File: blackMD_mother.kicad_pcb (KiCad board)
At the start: 2 copper layers, 99.1 x 99.1 mm, 19 parts

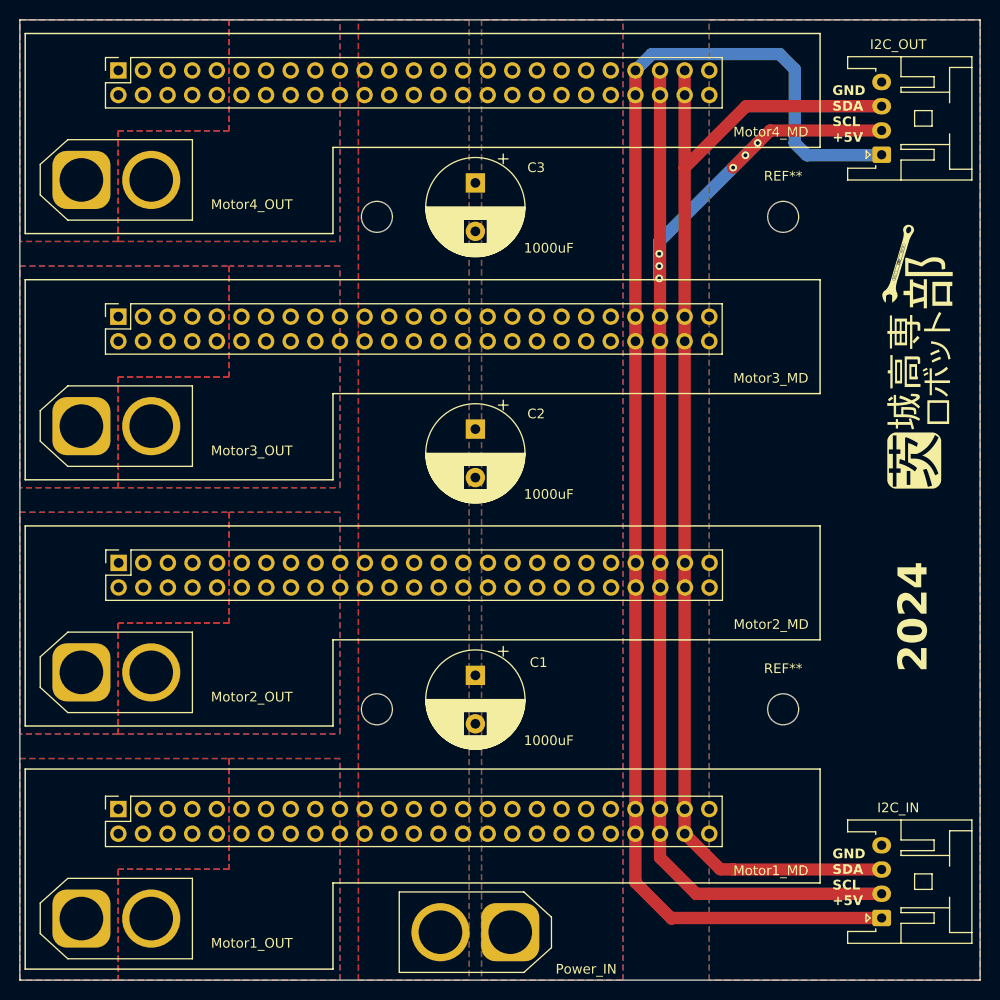
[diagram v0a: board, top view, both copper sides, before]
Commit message: change: fillet corners
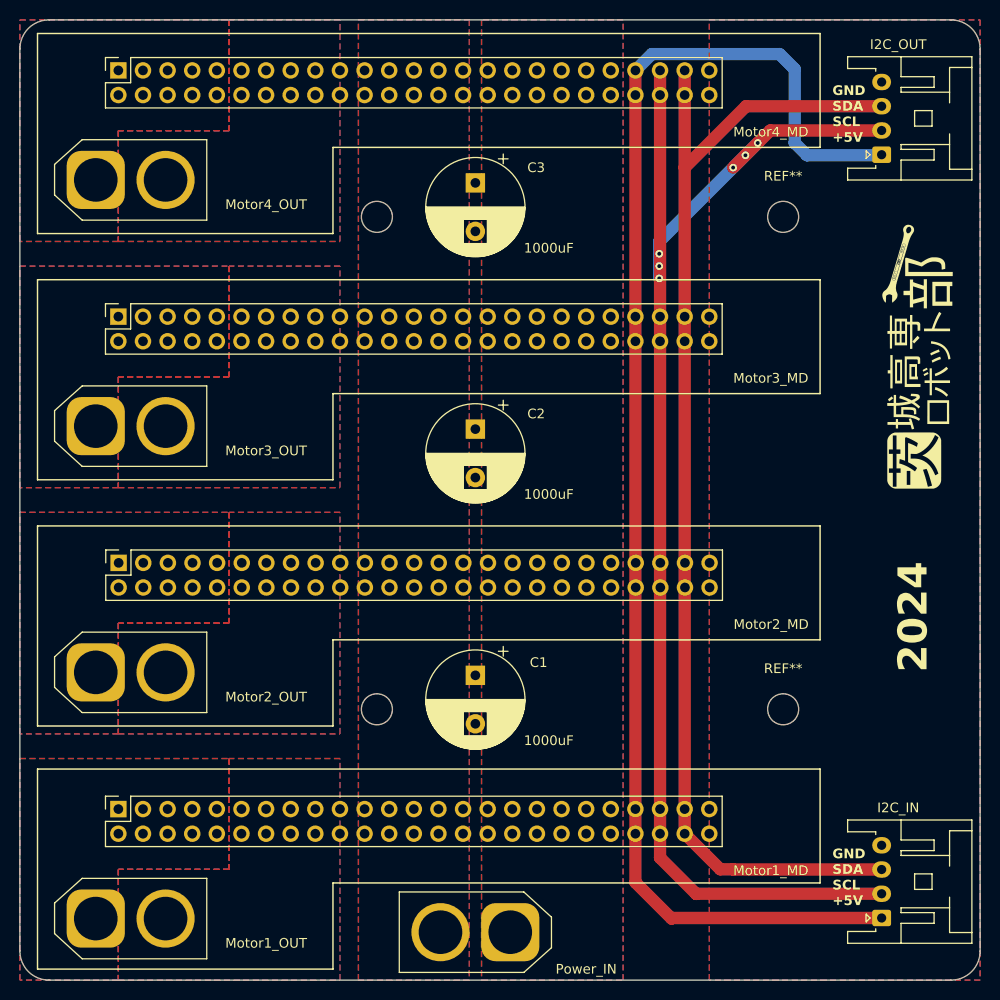
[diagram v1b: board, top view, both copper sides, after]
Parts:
- moved Motor1_OUT 1.48 mm to (100.6, 147.3)
- moved Motor2_OUT 1.48 mm to (100.6, 121.9)
- moved Motor3_OUT 1.48 mm to (100.6, 96.5)
- moved Motor4_OUT 1.48 mm to (100.6, 71.1)
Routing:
- added copper zone on B.Cu, net GND
- added copper zone on F.Cu, net GND
- removed copper zone on B.Cu, net (none)
- removed copper zone on F.Cu, net (none)
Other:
- outline, holes or cut-outs redrawn
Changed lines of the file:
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@@
       (sketchpadsonfab false)
       (subtractmaskfromsilk false)
-      (outputformat 4)
+      (outputformat 1)
       (mirror false)
       (drillshape 0)
@@
   )
   (footprint "Connector_AMASS:AMASS_XT60-F_1x02_P7.20mm_Vertical" (layer "F.Cu")
-    (at 99.141323 121.92)
+    (at 100.621323 121.92)
     (descr "AMASS female XT60, through hole, vertical, https://www.tme.eu/Document/2d152ced3b7a446066e6c419d84bb460/XT60%20SPEC.pdf")
     (tags "XT60 female vertical")
@@
   )
   (footprint "Connector_AMASS:AMASS_XT60-F_1x02_P7.20mm_Vertical" (layer "F.Cu")
-    (at 99.141323 71.12)
+    (at 100.621323 71.12)
     (descr "AMASS female XT60, through hole, vertical, https://www.tme.eu/Document/2d152ced3b7a446066e6c419d84bb460/XT60%20SPEC.pdf")
     (tags "XT60 female vertical")
@@
   )
   (footprint "Connector_AMASS:AMASS_XT60-F_1x02_P7.20mm_Vertical" (layer "F.Cu")
-    (at 99.141323 96.52)
+    (at 100.621323 96.52)
     (descr "AMASS female XT60, through hole, vertical, https://www.tme.eu/Document/2d152ced3b7a446066e6c419d84bb460/XT60%20SPEC.pdf")
     (tags "XT60 female vertical")
@@
   )
   (footprint "Connector_AMASS:AMASS_XT60-F_1x02_P7.20mm_Vertical" (layer "F.Cu")
-    (at 99.141323 147.32)
+    (at 100.621323 147.32)
     (descr "AMASS female XT60, through hole, vertical, https://www.tme.eu/Document/2d152ced3b7a446066e6c419d84bb460/XT60%20SPEC.pdf")
     (tags "XT60 female vertical")
@@
       (xy 125.091323 118.564677)
       (xy 125.091323 127.454677)
-      (xy 93.341323 127.454677)
-      (xy 93.341323 106.814677)
+      (xy 94.611323 127.454677)
+      (xy 94.611323 106.814677)
       (xy 175.341323 106.814677)
     )
@@
       (xy 125.091323 93.164677)
       (xy 125.091323 102.054677)
-      (xy 93.341323 102.054677)
-      (xy 93.341323 81.414677)
+      (xy 94.611323 102.054677)
+      (xy 94.611323 81.414677)
       (xy 175.341323 81.414677)
     )
@@
       (xy 125.091323 67.764677)
       (xy 125.091323 76.654677)
-      (xy 93.341323 76.654677)
-      (xy 93.341323 56.014677)
+      (xy 94.611323 76.654677)
+      (xy 94.611323 56.014677)
       (xy 175.341323 56.014677)
     )
@@
       (xy 125.091323 143.644677)
       (xy 125.091323 152.534677)
-      (xy 93.341323 152.534677)
-      (xy 93.341323 131.894677)
+      (xy 94.611323 152.534677)
+      (xy 94.611323 131.894677)
       (xy 175.341323 131.894677)
     )
     (stroke (width 0.15) (type solid)) (fill none) (layer "F.SilkS"))
-  (gr_poly
-    (pts
-      (xy 92.791323 153.67)
-      (xy 191.851323 153.67)
-      (xy 191.851323 54.61)
-      (xy 92.791323 54.61)
-    )
-    (stroke (width 0.1) (type solid)) (fill none) (layer "Edge.Cuts"))
+  (gr_arc (start 188.851323 54.61) (mid 190.972628 55.488688) (end 191.851323 57.61)
+    (stroke (width 0.1) (type default)) (layer "Edge.Cuts"))
+  (gr_line (start 92.791323 57.61) (end 92.791323 150.67)
+    (stroke (width 0.1) (type default)) (layer "Edge.Cuts"))
+  (gr_arc (start 95.791323 153.67) (mid 93.670003 152.79132) (end 92.791323 150.67)
+    (stroke (width 0.1) (type default)) (layer "Edge.Cuts"))
+  (gr_arc (start 92.791323 57.61) (mid 93.670004 55.488688) (end 95.791323 54.61)
+    (stroke (width 0.1) (type default)) (layer "Edge.Cuts"))
+  (gr_line (start 188.851323 54.61) (end 95.791323 54.61)
+    (stroke (width 0.1) (type default)) (layer "Edge.Cuts"))
+  (gr_arc (start 191.851323 150.67) (mid 190.972645 152.791328) (end 188.851323 153.67)
+    (stroke (width 0.1) (type default)) (layer "Edge.Cuts"))
+  (gr_line (start 95.791323 153.67) (end 188.851323 153.67)
+    (stroke (width 0.1) (type default)) (layer "Edge.Cuts"))
+  (gr_line (start 191.851323 150.67) (end 191.851323 57.61)
+    (stroke (width 0.1) (type default)) (layer "Edge.Cuts"))
   (gr_text "2024" (at 186.69 121.92 90) (layer "F.SilkS")
     (effects (font (size 3 3) (thickness 0.75) bold) (justify left bottom))
@@
     )
   )
-  (zone (net 0) (net_name "") (layers "F&B.Cu") (hatch edge 0.5)
+  (zone (net 10) (net_name "GND") (layers "F&B.Cu") (hatch edge 0.5)
     (connect_pads yes (clearance 0.5))
     (min_thickness 0.25) (filled_areas_thickness no)
-    (fill yes (thermal_gap 0.5) (thermal_bridge_width 1) (island_removal_mode 1) (island_area_min 10))
+    (fill yes (thermal_gap 0.5) (thermal_bridge_width 1))
     (polygon
       (pts

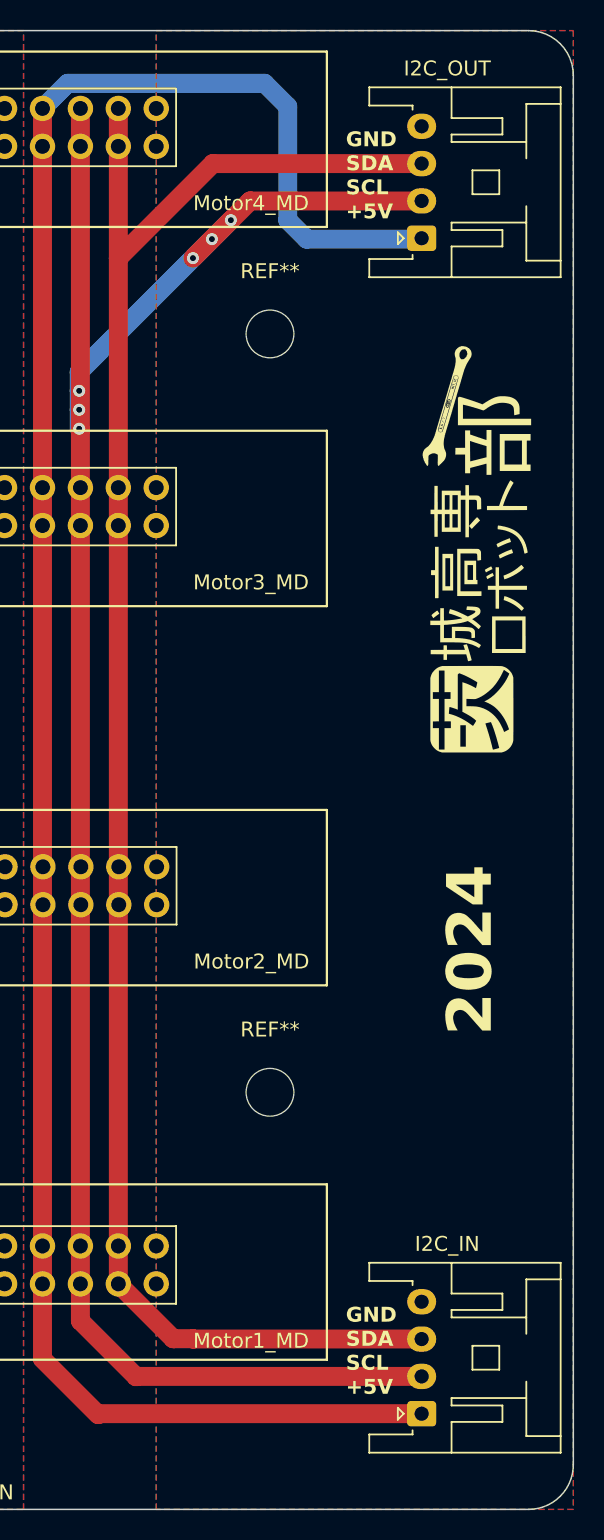
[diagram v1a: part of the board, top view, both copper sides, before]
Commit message: change: XAconnector, horizontal to vertical; This commit includes PDFs & GBRs changes
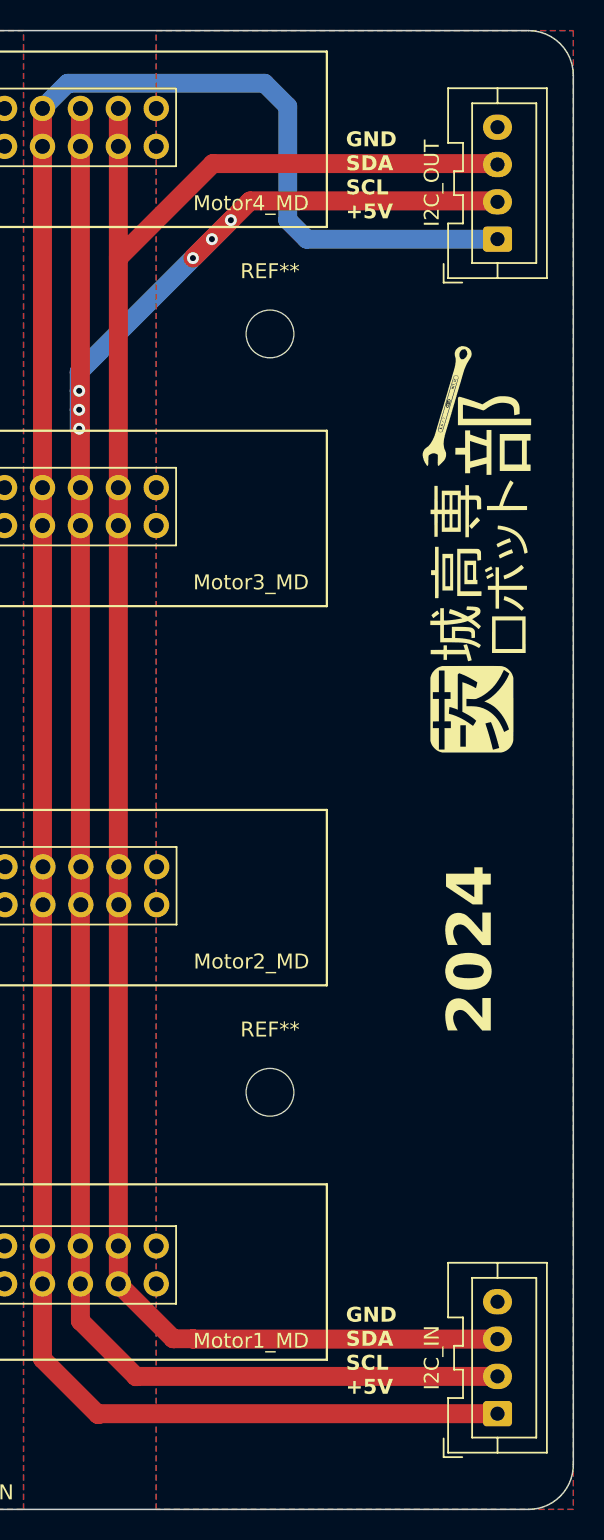
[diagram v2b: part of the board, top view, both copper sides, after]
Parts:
- I2C_IN, I2C_OUT: footprint Connector_JST:JST_XA_S04B-XASK-1_1x04_P2.50mm_Horizontal -> Connector_JST:JST_XA_B04B-XASK-1_1x04_P2.50mm_Vertical
- moved I2C_OUT 5.08 mm to (186.8, 68.6)
- moved I2C_IN 5.08 mm to (186.8, 147.3)
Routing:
- net SDA: track 123.5 -> 133.7 mm
- net SCL: track 140.7 -> 150.9 mm
- net +5V: track 145.6 -> 155.8 mm
